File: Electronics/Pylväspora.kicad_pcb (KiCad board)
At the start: 2 copper layers, 29.8 x 35 mm, 19 parts, among them SW1 SW_Push, SW2 SW_Push, U1 ATtiny814-SS, U2 AMS1117-3.3

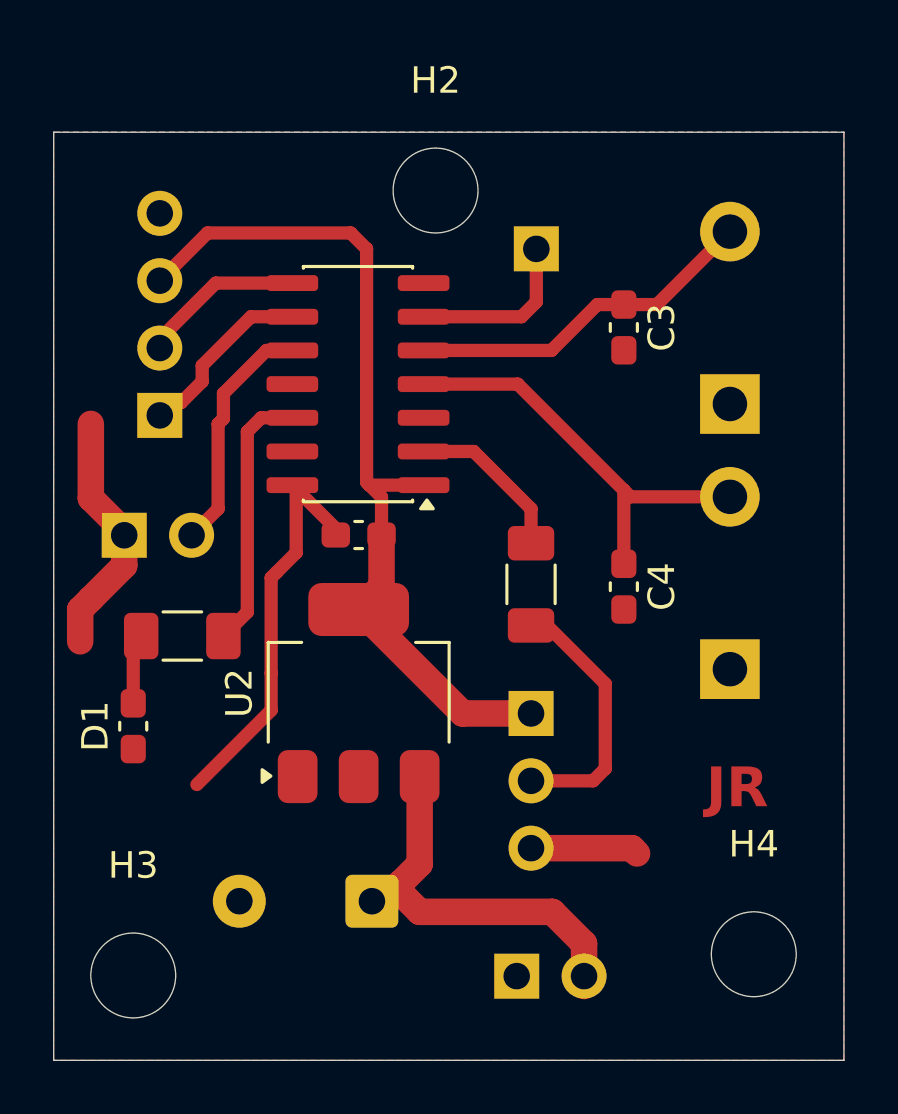
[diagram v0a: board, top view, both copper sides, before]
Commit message: Corrected jst model footprints
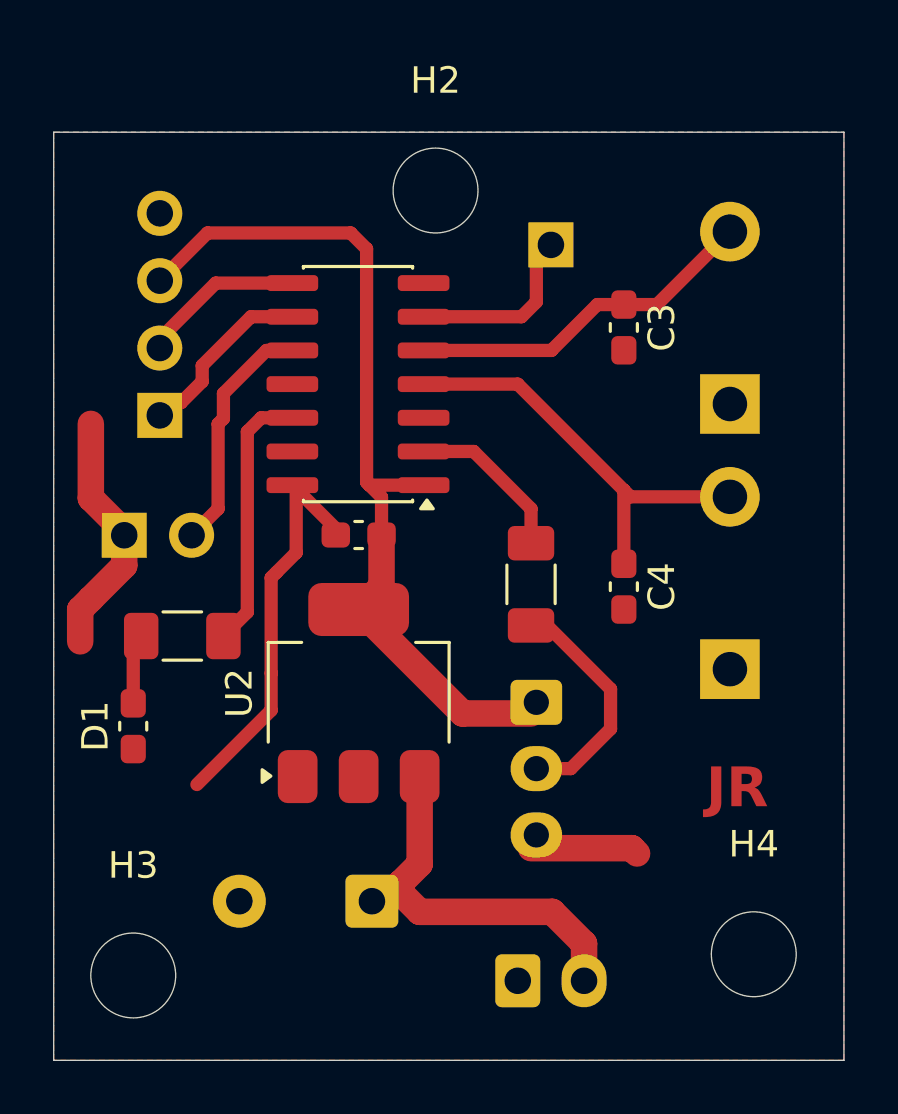
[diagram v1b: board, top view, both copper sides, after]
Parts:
- Feedback1: footprint Connector_PinSocket_2.54mm:PinSocket_1x03_P2.54mm_Vertical -> Connector_JST:JST_EH_B3B-EH-A_1x03_P2.50mm_Vertical
- PWM_out1: footprint Connector_PinSocket_2.54mm:PinSocket_1x01_P2.54mm_Vertical -> Connector_PinHeader_2.54mm:PinHeader_1x01_P2.54mm_Vertical
- PWR1: footprint Connector_PinSocket_2.54mm:PinSocket_1x02_P2.54mm_Vertical -> Connector_JST:JST_EH_B2B-EH-A_1x02_P2.50mm_Vertical
- moved PWM_out1 0.57 mm to (154.8, 80.2), turned to 0 degrees
- moved Feedback1 0.47 mm to (154.2, 97.5), turned to -90 degrees
- moved PWR1 0.18 mm to (153.5, 108.0), turned to 0 degrees
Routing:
- net Net-(Feedback1-Pin_2): track 9.90 -> 8.92 mm

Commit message: Small schematic and layout fix
Forgot a pullup resistor from hall input, added 4.7k pullup. Fixed incorrect measurement of RPM and increased update frequency in software
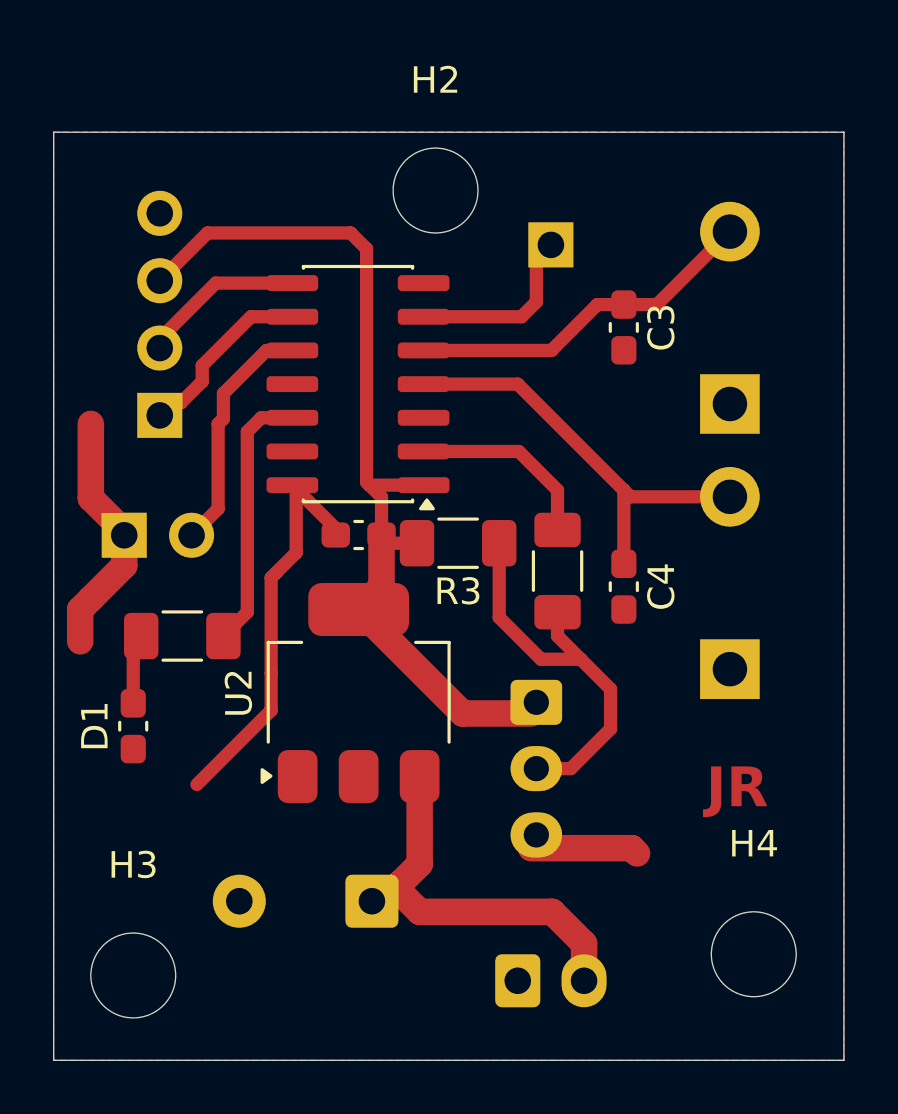
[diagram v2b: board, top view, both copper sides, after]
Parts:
- added R3: 4.7k, Resistor_SMD:R_1206_3216Metric_Pad1.30x1.75mm_HandSolder, F.Cu at (151.2, 91.5)
- C1: value C -> 100u
- C2: value C -> 10u
- C3, C4: value C -> 10n
- R1, R2: value R -> 1k
- moved R1 1.12 mm to (155.0, 92.5)
- renumbered Feedback1 to Hallinput1
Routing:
- net Net-(Hallinput1-Pin_2): track 8.92 -> 15.2 mm
- net 3.3V: track 33.1 -> 34.6 mm
- net PA4: track 6.24 -> 7.15 mm
